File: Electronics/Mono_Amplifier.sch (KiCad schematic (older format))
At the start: 14 parts

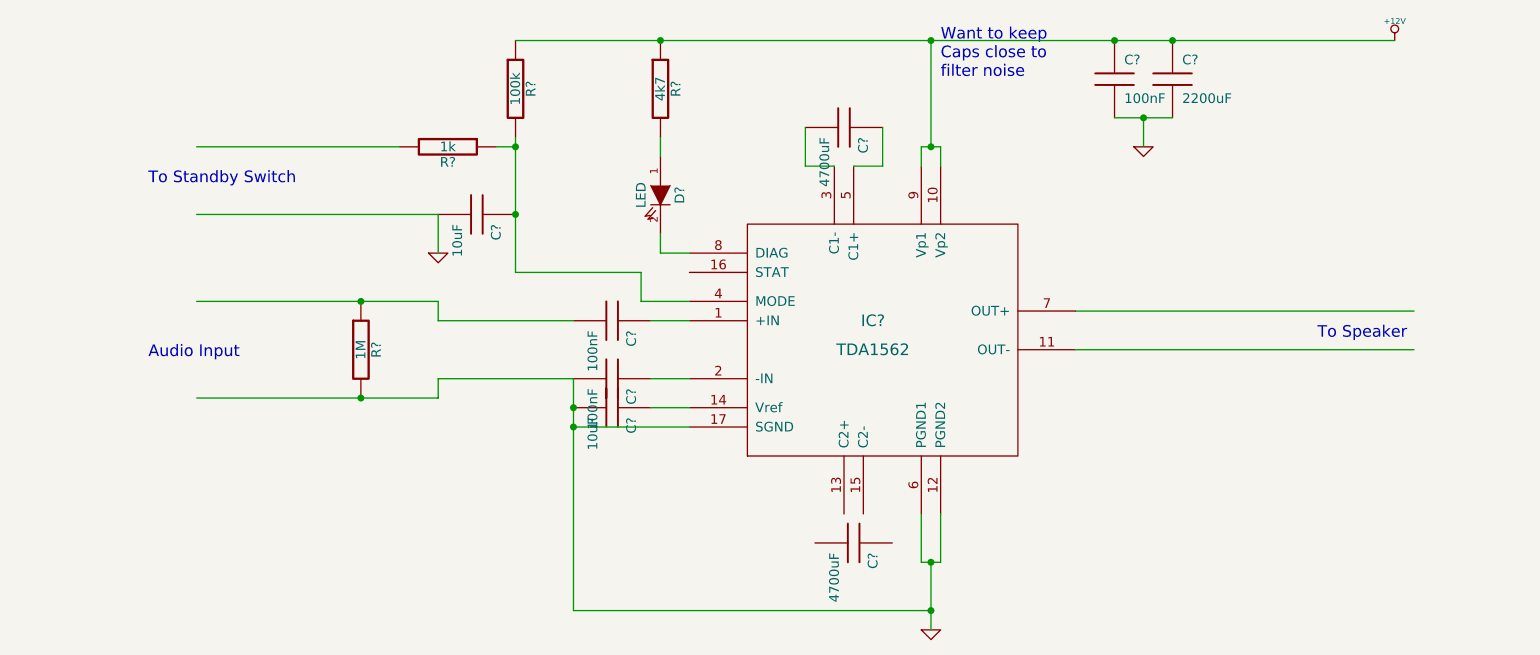
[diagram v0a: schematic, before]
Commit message: Added a few connectors Cleaning up some of the labels
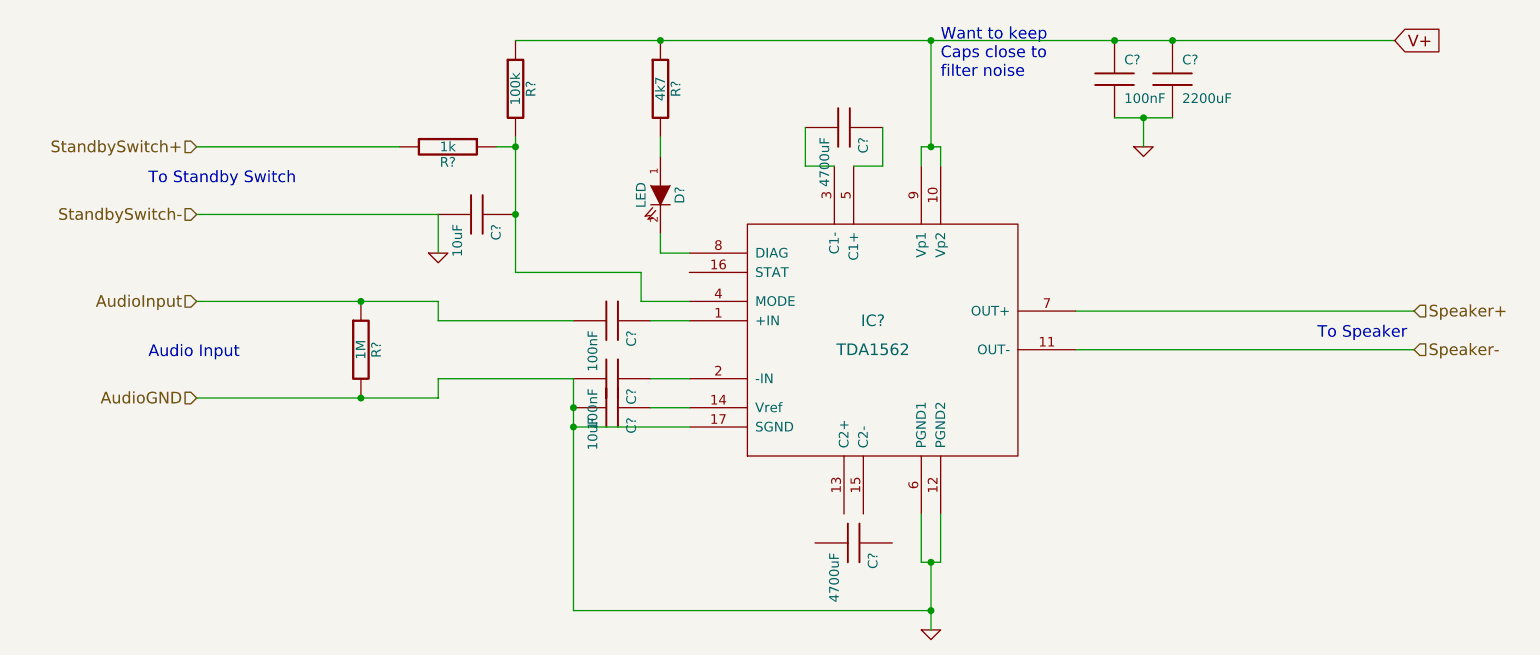
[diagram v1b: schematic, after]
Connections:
- net labels added: AudioGND, AudioInput, Speaker+, Speaker-, StandbySwitch+, StandbySwitch-, V+
- net labels removed: +12V
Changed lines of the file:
@@
-EESchema Schematic File Version 2  date 8/2/2012 12:00:58 PM
+EESchema Schematic File Version 2  date 8/2/2012 3:30:21 PM
 LIBS:power
 LIBS:device
@@
 $Descr A4 11700 8267
 encoding utf-8
-Sheet 2 2
+Sheet 4 4
 Title ""
 Date "2 aug 2012"
@@
 Comment4 ""
 $EndDescr
+Text GLabel 8700 2000 2    60   Input ~ 0
+V+
+Text HLabel 2500 2900 0    60   Input ~ 0
+StandbySwitch-
+Text HLabel 2500 2550 0    60   Input ~ 0
+StandbySwitch+
+Wire Wire Line
+	3550 2550 2500 2550
+Text HLabel 2500 3850 0    60   Input ~ 0
+AudioGND
+Text HLabel 2500 3350 0    60   Input ~ 0
+AudioInput
+Text HLabel 8800 3600 2    60   Input ~ 0
+Speaker-
+Text HLabel 8800 3400 2    60   Input ~ 0
+Speaker+
 Text Notes 6350 2200 0    60   ~ 0
 Want to keep\nCaps close to \nfilter noise
@@
 Wire Wire Line
 	3750 3750 3750 3850
-Wire Wire Line
-	3550 2550 2500 2550
 Connection ~ 4150 2550
 Wire Wire Line
@@
 U 1 1 501AB189
 P 3350 3600
+AR Path="/501AA789/501AB189" Ref="R?"  Part="1"
+AR Path="/501ABAFF/501AB189" Ref="R?"  Part="1"
 F 0 "R?" V 3430 3600 50  0000 C CNN
 F 1 "1M" V 3350 3600 50  0000 C CNN
@@
 U 1 1 501AB131
 P 3750 3100
+AR Path="/501AA789/501AB131" Ref="#PWR?"  Part="1"
+AR Path="/501ABAFF/501AB131" Ref="#PWR?"  Part="1"
 F 0 "#PWR?" H 3750 3100 30  0001 C CNN
 F 1 "GND" H 3750 3030 30  0001 C CNN
@@
 U 1 1 501AB0FF
 P 3950 2900
+AR Path="/501AA789/501AB0FF" Ref="C?"  Part="1"
+AR Path="/501ABAFF/501AB0FF" Ref="C?"  Part="1"
 F 0 "C?" H 4000 3000 50  0000 L CNN
 F 1 "10uF" H 4000 2800 50  0000 L CNN
@@
 U 1 1 501AB0EA
 P 3800 2550
+AR Path="/501AA789/501AB0EA" Ref="R?"  Part="1"
+AR Path="/501ABAFF/501AB0EA" Ref="R?"  Part="1"
 F 0 "R?" V 3880 2550 50  0000 C CNN
 F 1 "1k" V 3800 2550 50  0000 C CNN
@@
 U 1 1 501AB09B
 P 4150 2250
+AR Path="/501AA789/501AB09B" Ref="R?"  Part="1"
+AR Path="/501ABAFF/501AB09B" Ref="R?"  Part="1"
 F 0 "R?" V 4230 2250 50  0000 C CNN
 F 1 "100k" V 4150 2250 50  0000 C CNN
@@
 $EndComp
 $Comp
-L +12V #PWR?
-U 1 1 501AB062
-P 8700 2000
-F 0 "#PWR?" H 8700 1950 20  0001 C CNN
-F 1 "+12V" H 8700 2100 30  0000 C CNN
-	1    8700 2000
-	1    0    0    -1
-$EndComp
-$Comp
 L R R?
 U 1 1 501AB045
 P 4900 2250
+AR Path="/501AA789/501AB045" Ref="R?"  Part="1"
+AR Path="/501ABAFF/501AB045" Ref="R?"  Part="1"
 F 0 "R?" V 4980 2250 50  0000 C CNN
 F 1 "4k7" V 4900 2250 50  0000 C CNN
@@
 U 1 1 501AB020
 P 4900 2800
+AR Path="/501AA789/501AB020" Ref="D?"  Part="1"
+AR Path="/501ABAFF/501AB020" Ref="D?"  Part="1"
 F 0 "D?" H 4900 2900 50  0000 C CNN
 F 1 "LED" H 4900 2700 50  0000 C CNN
@@
 U 1 1 501AAF92
 P 7400 2550
+AR Path="/501AA789/501AAF92" Ref="#PWR?"  Part="1"
+AR Path="/501ABAFF/501AAF92" Ref="#PWR?"  Part="1"
 F 0 "#PWR?" H 7400 2550 30  0001 C CNN
 F 1 "GND" H 7400 2480 30  0001 C CNN
@@
 U 1 1 501AAF74
 P 6300 5050
+AR Path="/501AA789/501AAF74" Ref="#PWR?"  Part="1"
+AR Path="/501ABAFF/501AAF74" Ref="#PWR?"  Part="1"
 F 0 "#PWR?" H 6300 5050 30  0001 C CNN
 F 1 "GND" H 6300 4980 30  0001 C CNN
@@
 U 1 1 501AAE97
 P 7550 2200
+AR Path="/501AA789/501AAE97" Ref="C?"  Part="1"
+AR Path="/501ABAFF/501AAE97" Ref="C?"  Part="1"
 F 0 "C?" H 7600 2300 50  0000 L CNN
 F 1 "2200uF" H 7600 2100 50  0000 L CNN
@@
 U 1 1 501AAE33
 P 7250 2200
+AR Path="/501AA789/501AAE33" Ref="C?"  Part="1"
+AR Path="/501ABAFF/501AAE33" Ref="C?"  Part="1"
 F 0 "C?" H 7300 2300 50  0000 L CNN
 F 1 "100nF" H 7300 2100 50  0000 L CNN
@@
 U 1 1 501AAE22
 P 4650 3900
+AR Path="/501AA789/501AAE22" Ref="C?"  Part="1"
+AR Path="/501ABAFF/501AAE22" Ref="C?"  Part="1"
 F 0 "C?" H 4700 4000 50  0000 L CNN
 F 1 "10uF" H 4700 3800 50  0000 L CNN
@@
 U 1 1 501AAE14
 P 4650 3750
+AR Path="/501AA789/501AAE14" Ref="C?"  Part="1"
+AR Path="/501ABAFF/501AAE14" Ref="C?"  Part="1"
 F 0 "C?" H 4700 3850 50  0000 L CNN
 F 1 "100nF" H 4700 3650 50  0000 L CNN
@@
 U 1 1 501AAE08
 P 4650 3450
+AR Path="/501AA789/501AAE08" Ref="C?"  Part="1"
+AR Path="/501ABAFF/501AAE08" Ref="C?"  Part="1"
 F 0 "C?" H 4700 3550 50  0000 L CNN
 F 1 "100nF" H 4700 3350 50  0000 L CNN
@@
 U 1 1 501AADFF
 P 5900 4600
+AR Path="/501AA789/501AADFF" Ref="C?"  Part="1"
+AR Path="/501ABAFF/501AADFF" Ref="C?"  Part="1"
 F 0 "C?" H 5950 4700 50  0000 L CNN
 F 1 "4700uF" H 5950 4500 50  0000 L CNN
@@
 U 1 1 501AADE8
 P 5850 2450
+AR Path="/501AA789/501AADE8" Ref="C?"  Part="1"
+AR Path="/501ABAFF/501AADE8" Ref="C?"  Part="1"
 F 0 "C?" H 5900 2550 50  0000 L CNN
 F 1 "4700uF" H 5900 2350 50  0000 L CNN
@@
 U 1 1 501AA7BF
 P 6000 3500
+AR Path="/501AA789/501AA7BF" Ref="IC?"  Part="1"
+AR Path="/501ABAFF/501AA7BF" Ref="IC?"  Part="1"
 F 0 "IC?" H 6000 3550 60  0000 C CNN
 F 1 "TDA1562" H 6000 3400 60  0000 C CNN

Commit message: I think the first draft is done. Next step is to get a rough PCB setup.
Still need to find componets for all of the
caps, resistors, fuse, and connectors
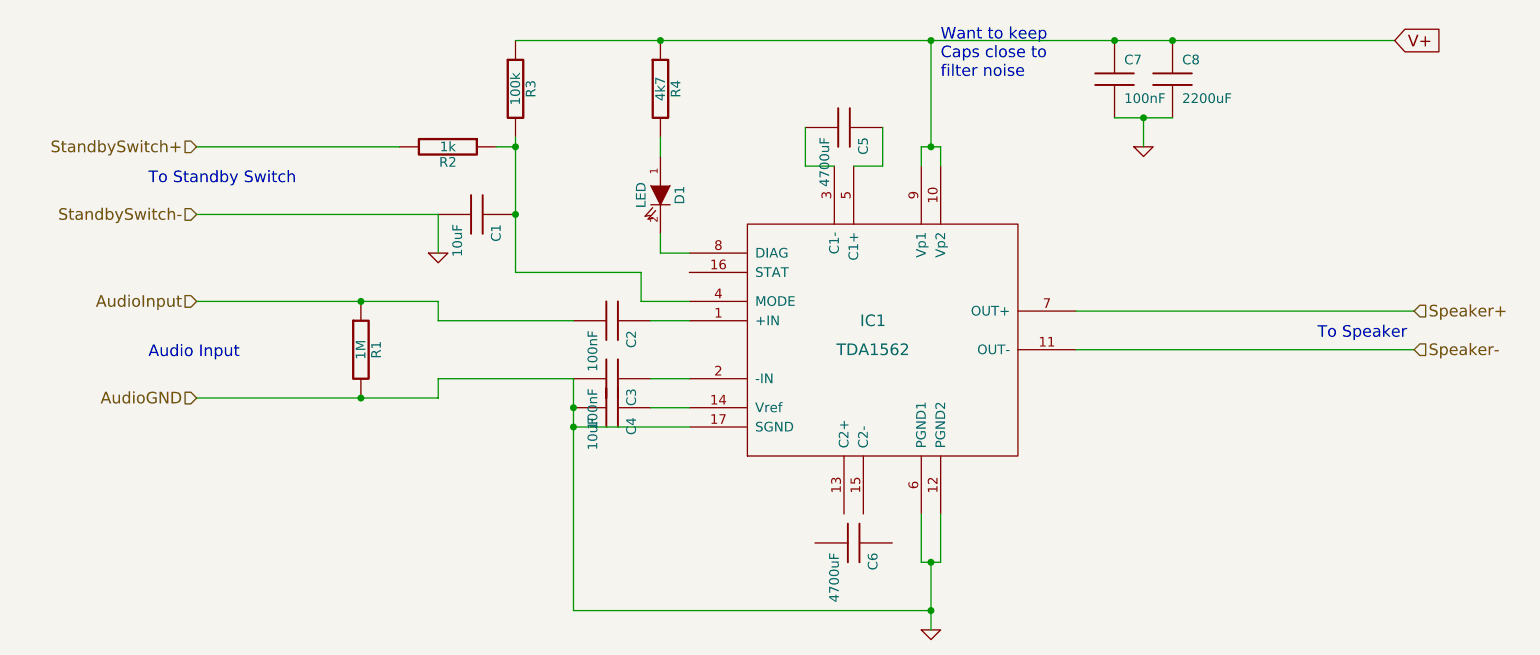
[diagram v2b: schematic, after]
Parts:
- gave numbers to parts that had none: 14
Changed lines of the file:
@@
-EESchema Schematic File Version 2  date 8/2/2012 3:30:21 PM
+EESchema Schematic File Version 2  date 8/2/2012 4:04:56 PM
 LIBS:power
 LIBS:device
@@
 $Descr A4 11700 8267
 encoding utf-8
-Sheet 4 4
+Sheet 4 5
 Title ""
 Date "2 aug 2012"
@@
 Audio Input
 $Comp
-L R R?
+L R R5
 U 1 1 501AB189
 P 3350 3600
-AR Path="/501AA789/501AB189" Ref="R?"  Part="1"
-AR Path="/501ABAFF/501AB189" Ref="R?"  Part="1"
-F 0 "R?" V 3430 3600 50  0000 C CNN
+AR Path="/501AA789/501AB189" Ref="R5"  Part="1"
+AR Path="/501ABAFF/501AB189" Ref="R1"  Part="1"
+F 0 "R1" V 3430 3600 50  0000 C CNN
 F 1 "1M" V 3350 3600 50  0000 C CNN
 	1    3350 3600
@@
 To Standby Switch
 $Comp
-L GND #PWR?
+L GND #PWR5
 U 1 1 501AB131
 P 3750 3100
-AR Path="/501AA789/501AB131" Ref="#PWR?"  Part="1"
-AR Path="/501ABAFF/501AB131" Ref="#PWR?"  Part="1"
-F 0 "#PWR?" H 3750 3100 30  0001 C CNN
+AR Path="/501AA789/501AB131" Ref="#PWR5"  Part="1"
+AR Path="/501ABAFF/501AB131" Ref="#PWR2"  Part="1"
+F 0 "#PWR2" H 3750 3100 30  0001 C CNN
 F 1 "GND" H 3750 3030 30  0001 C CNN
 	1    3750 3100
@@
 $EndComp
 $Comp
-L C C?
+L C C9
 U 1 1 501AB0FF
 P 3950 2900
-AR Path="/501AA789/501AB0FF" Ref="C?"  Part="1"
-AR Path="/501ABAFF/501AB0FF" Ref="C?"  Part="1"
-F 0 "C?" H 4000 3000 50  0000 L CNN
+AR Path="/501AA789/501AB0FF" Ref="C9"  Part="1"
+AR Path="/501ABAFF/501AB0FF" Ref="C1"  Part="1"
+F 0 "C1" H 4000 3000 50  0000 L CNN
 F 1 "10uF" H 4000 2800 50  0000 L CNN
 	1    3950 2900
@@
 $EndComp
 $Comp
-L R R?
+L R R6
 U 1 1 501AB0EA
 P 3800 2550
-AR Path="/501AA789/501AB0EA" Ref="R?"  Part="1"
-AR Path="/501ABAFF/501AB0EA" Ref="R?"  Part="1"
-F 0 "R?" V 3880 2550 50  0000 C CNN
+AR Path="/501AA789/501AB0EA" Ref="R6"  Part="1"
+AR Path="/501ABAFF/501AB0EA" Ref="R2"  Part="1"
+F 0 "R2" V 3880 2550 50  0000 C CNN
 F 1 "1k" V 3800 2550 50  0000 C CNN
 	1    3800 2550
@@
 $EndComp
 $Comp
-L R R?
+L R R7
 U 1 1 501AB09B
 P 4150 2250
-AR Path="/501AA789/501AB09B" Ref="R?"  Part="1"
-AR Path="/501ABAFF/501AB09B" Ref="R?"  Part="1"
-F 0 "R?" V 4230 2250 50  0000 C CNN
+AR Path="/501AA789/501AB09B" Ref="R7"  Part="1"
+AR Path="/501ABAFF/501AB09B" Ref="R3"  Part="1"
+F 0 "R3" V 4230 2250 50  0000 C CNN
 F 1 "100k" V 4150 2250 50  0000 C CNN
 	1    4150 2250
@@
 $EndComp
 $Comp
-L R R?
+L R R8
 U 1 1 501AB045
 P 4900 2250
-AR Path="/501AA789/501AB045" Ref="R?"  Part="1"
-AR Path="/501ABAFF/501AB045" Ref="R?"  Part="1"
-F 0 "R?" V 4980 2250 50  0000 C CNN
+AR Path="/501AA789/501AB045" Ref="R8"  Part="1"
+AR Path="/501ABAFF/501AB045" Ref="R4"  Part="1"
+F 0 "R4" V 4980 2250 50  0000 C CNN
 F 1 "4k7" V 4900 2250 50  0000 C CNN
 	1    4900 2250
@@
 $EndComp
 $Comp
-L LED D?
+L LED D2
 U 1 1 501AB020
 P 4900 2800
-AR Path="/501AA789/501AB020" Ref="D?"  Part="1"
-AR Path="/501ABAFF/501AB020" Ref="D?"  Part="1"
-F 0 "D?" H 4900 2900 50  0000 C CNN
+AR Path="/501AA789/501AB020" Ref="D2"  Part="1"
+AR Path="/501ABAFF/501AB020" Ref="D1"  Part="1"
+F 0 "D1" H 4900 2900 50  0000 C CNN
 F 1 "LED" H 4900 2700 50  0000 C CNN
 	1    4900 2800
@@
 $EndComp
 $Comp
-L GND #PWR?
+L GND #PWR7
 U 1 1 501AAF92
 P 7400 2550
-AR Path="/501AA789/501AAF92" Ref="#PWR?"  Part="1"
-AR Path="/501ABAFF/501AAF92" Ref="#PWR?"  Part="1"
-F 0 "#PWR?" H 7400 2550 30  0001 C CNN
+AR Path="/501AA789/501AAF92" Ref="#PWR7"  Part="1"
+AR Path="/501ABAFF/501AAF92" Ref="#PWR4"  Part="1"
+F 0 "#PWR4" H 7400 2550 30  0001 C CNN
 F 1 "GND" H 7400 2480 30  0001 C CNN
 	1    7400 2550
@@
 $EndComp
 $Comp
-L GND #PWR?
+L GND #PWR6
 U 1 1 501AAF74
 P 6300 5050
-AR Path="/501AA789/501AAF74" Ref="#PWR?"  Part="1"
-AR Path="/501ABAFF/501AAF74" Ref="#PWR?"  Part="1"
-F 0 "#PWR?" H 6300 5050 30  0001 C CNN
+AR Path="/501AA789/501AAF74" Ref="#PWR6"  Part="1"
+AR Path="/501ABAFF/501AAF74" Ref="#PWR3"  Part="1"
+F 0 "#PWR3" H 6300 5050 30  0001 C CNN
 F 1 "GND" H 6300 4980 30  0001 C CNN
 	1    6300 5050
@@
 $EndComp
 $Comp
-L C C?
+L C C16
 U 1 1 501AAE97
 P 7550 2200
-AR Path="/501AA789/501AAE97" Ref="C?"  Part="1"
-AR Path="/501ABAFF/501AAE97" Ref="C?"  Part="1"
-F 0 "C?" H 7600 2300 50  0000 L CNN
+AR Path="/501AA789/501AAE97" Ref="C16"  Part="1"
+AR Path="/501ABAFF/501AAE97" Ref="C8"  Part="1"
+F 0 "C8" H 7600 2300 50  0000 L CNN
 F 1 "2200uF" H 7600 2100 50  0000 L CNN
 	1    7550 2200
@@
 $EndComp
 $Comp
-L C C?
+L C C15
 U 1 1 501AAE33
 P 7250 2200
-AR Path="/501AA789/501AAE33" Ref="C?"  Part="1"
-AR Path="/501ABAFF/501AAE33" Ref="C?"  Part="1"
-F 0 "C?" H 7300 2300 50  0000 L CNN
+AR Path="/501AA789/501AAE33" Ref="C15"  Part="1"
+AR Path="/501ABAFF/501AAE33" Ref="C7"  Part="1"
+F 0 "C7" H 7300 2300 50  0000 L CNN
 F 1 "100nF" H 7300 2100 50  0000 L CNN
 	1    7250 2200
@@
 $EndComp
 $Comp
-L C C?
+L C C12
 U 1 1 501AAE22
 P 4650 3900
-AR Path="/501AA789/501AAE22" Ref="C?"  Part="1"
-AR Path="/501ABAFF/501AAE22" Ref="C?"  Part="1"
-F 0 "C?" H 4700 4000 50  0000 L CNN
+AR Path="/501AA789/501AAE22" Ref="C12"  Part="1"
+AR Path="/501ABAFF/501AAE22" Ref="C4"  Part="1"
+F 0 "C4" H 4700 4000 50  0000 L CNN
 F 1 "10uF" H 4700 3800 50  0000 L CNN
 	1    4650 3900
@@
 $EndComp
 $Comp
-L C C?
+L C C11
 U 1 1 501AAE14
 P 4650 3750
-AR Path="/501AA789/501AAE14" Ref="C?"  Part="1"
-AR Path="/501ABAFF/501AAE14" Ref="C?"  Part="1"
-F 0 "C?" H 4700 3850 50  0000 L CNN
+AR Path="/501AA789/501AAE14" Ref="C11"  Part="1"
+AR Path="/501ABAFF/501AAE14" Ref="C3"  Part="1"
+F 0 "C3" H 4700 3850 50  0000 L CNN
 F 1 "100nF" H 4700 3650 50  0000 L CNN
 	1    4650 3750
@@
 $EndComp
 $Comp
-L C C?
+L C C10
 U 1 1 501AAE08
 P 4650 3450
-AR Path="/501AA789/501AAE08" Ref="C?"  Part="1"
-AR Path="/501ABAFF/501AAE08" Ref="C?"  Part="1"
-F 0 "C?" H 4700 3550 50  0000 L CNN
+AR Path="/501AA789/501AAE08" Ref="C10"  Part="1"
+AR Path="/501ABAFF/501AAE08" Ref="C2"  Part="1"
+F 0 "C2" H 4700 3550 50  0000 L CNN
 F 1 "100nF" H 4700 3350 50  0000 L CNN
 	1    4650 3450
@@
 $EndComp
 $Comp
-L C C?
+L C C14
 U 1 1 501AADFF
 P 5900 4600
-AR Path="/501AA789/501AADFF" Ref="C?"  Part="1"
-AR Path="/501ABAFF/501AADFF" Ref="C?"  Part="1"
-F 0 "C?" H 5950 4700 50  0000 L CNN
+AR Path="/501AA789/501AADFF" Ref="C14"  Part="1"
+AR Path="/501ABAFF/501AADFF" Ref="C6"  Part="1"
+F 0 "C6" H 5950 4700 50  0000 L CNN
 F 1 "4700uF" H 5950 4500 50  0000 L CNN
 	1    5900 4600
@@
 $EndComp
 $Comp
-L C C?
+L C C13
 U 1 1 501AADE8
 P 5850 2450
-AR Path="/501AA789/501AADE8" Ref="C?"  Part="1"
-AR Path="/501ABAFF/501AADE8" Ref="C?"  Part="1"
-F 0 "C?" H 5900 2550 50  0000 L CNN
+AR Path="/501AA789/501AADE8" Ref="C13"  Part="1"
+AR Path="/501ABAFF/501AADE8" Ref="C5"  Part="1"
+F 0 "C5" H 5900 2550 50  0000 L CNN
 F 1 "4700uF" H 5900 2350 50  0000 L CNN
 	1    5850 2450
@@
 $EndComp
 $Comp
-L TDA1562 IC?
+L TDA1562 IC2
 U 1 1 501AA7BF
 P 6000 3500
-AR Path="/501AA789/501AA7BF" Ref="IC?"  Part="1"
-AR Path="/501ABAFF/501AA7BF" Ref="IC?"  Part="1"
-F 0 "IC?" H 6000 3550 60  0000 C CNN
+AR Path="/501AA789/501AA7BF" Ref="IC2"  Part="1"
+AR Path="/501ABAFF/501AA7BF" Ref="IC1"  Part="1"
+F 0 "IC1" H 6000 3550 60  0000 C CNN
 F 1 "TDA1562" H 6000 3400 60  0000 C CNN
 	1    6000 3500
